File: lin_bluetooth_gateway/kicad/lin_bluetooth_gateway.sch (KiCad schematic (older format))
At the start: 9 parts, among them P1 MOLEX-0431603103, P2 MOLEX-0431603103, P4 CONN_01X03, U1 MCP2050, U2 BL652

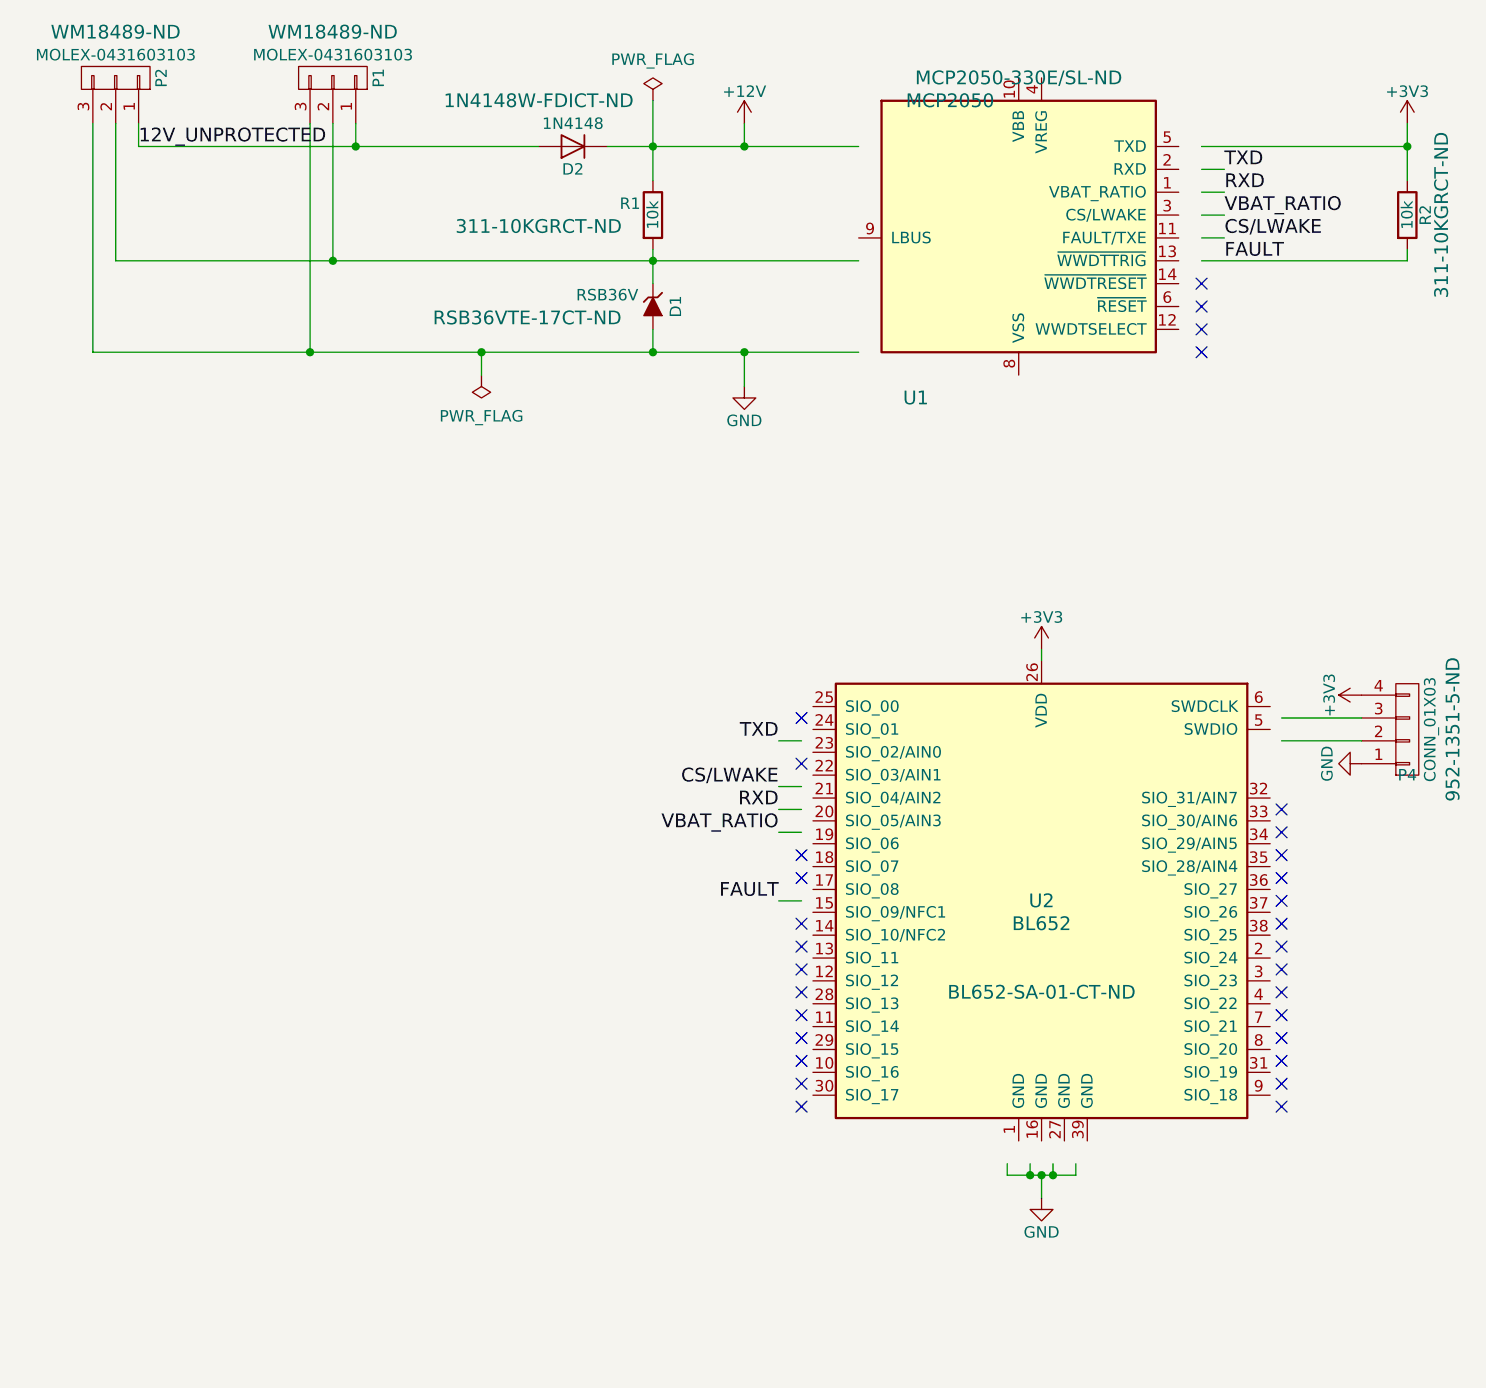
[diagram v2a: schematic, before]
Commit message: Moving MCP2050 symbol to "microchip" library
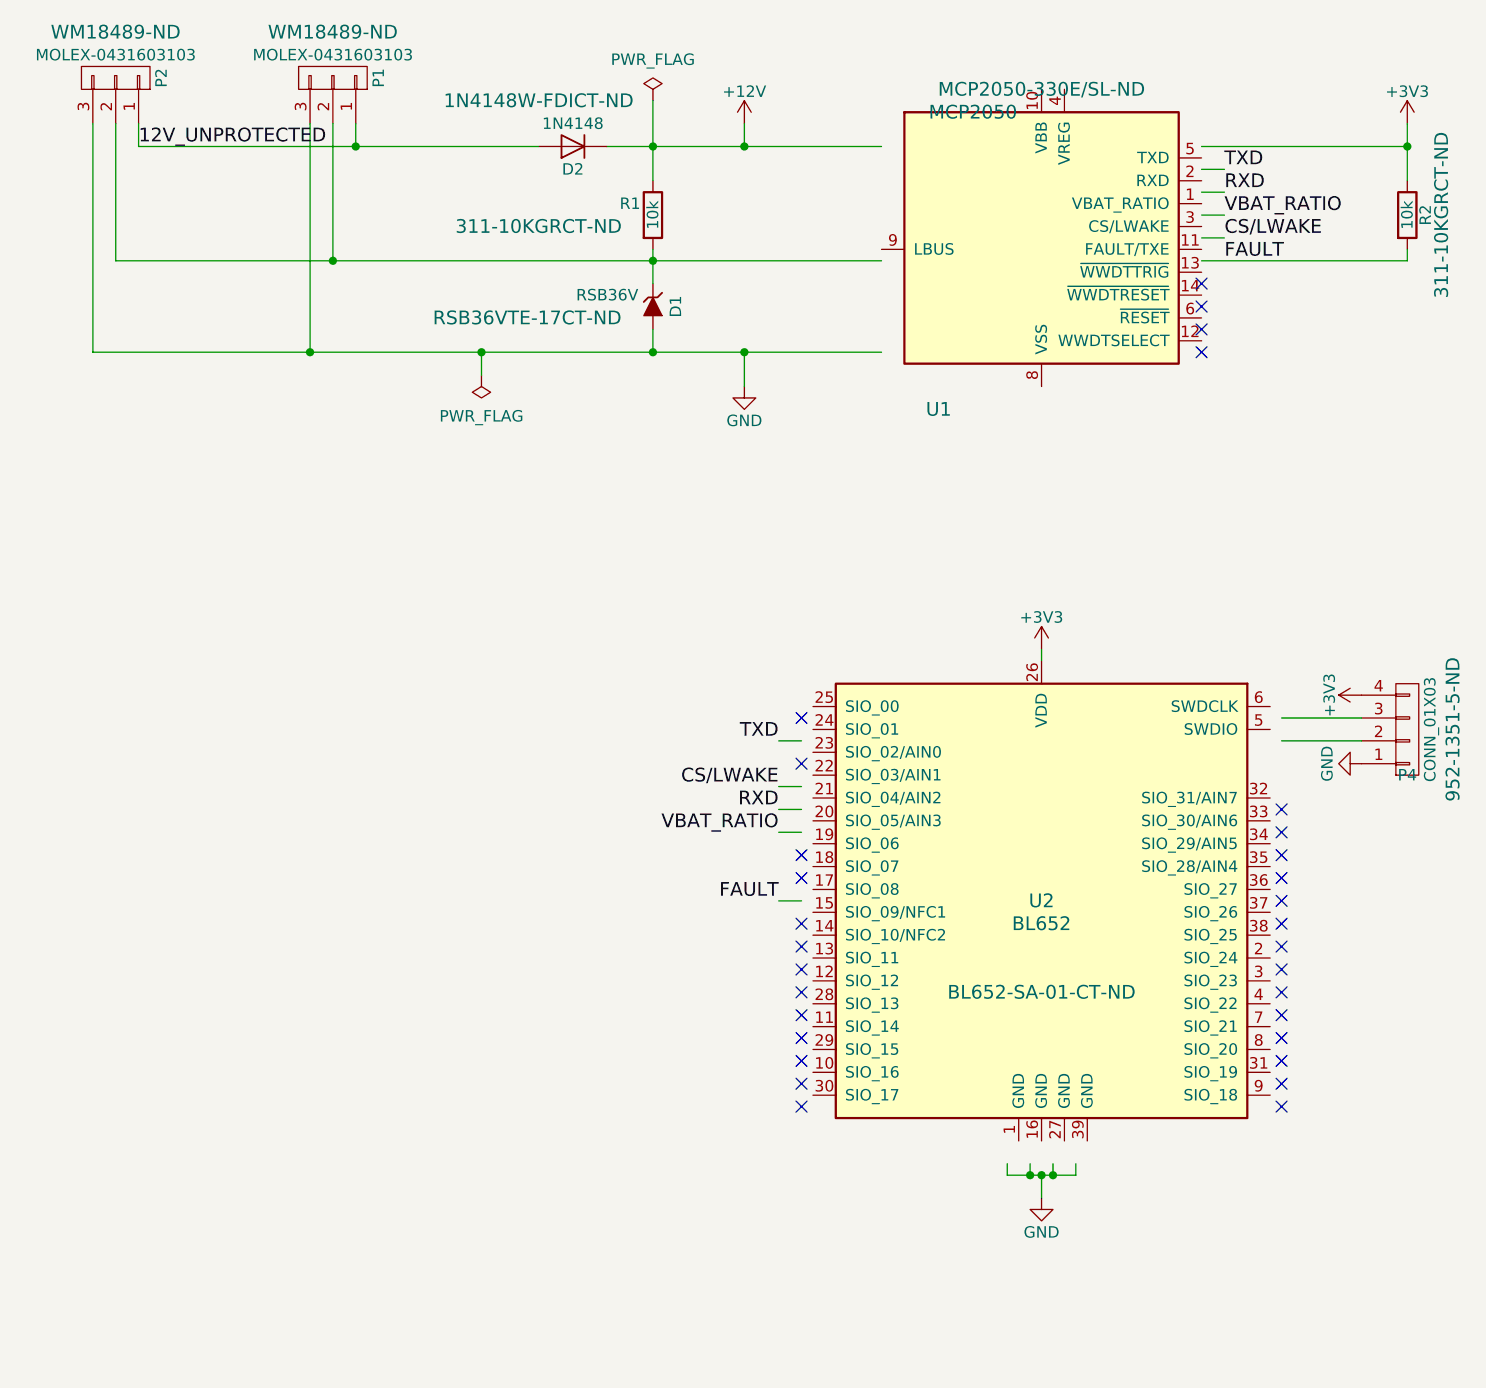
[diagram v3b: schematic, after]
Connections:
- wire segments 38 -> 53
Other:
- moved on the sheet: U1
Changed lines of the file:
@@
 LIBS:valves
 LIBS:laird
-LIBS:mcp2050
 LIBS:lin_bluetooth_gateway-cache
 EELAYER 25 0
@@
 L MCP2050 U1
 U 1 1 5807224D
-P 5350 1850
-F 0 "U1" H 4900 1150 60  0000 C CNN
-F 1 "MCP2050" H 5050 2450 60  0000 C CNN
-F 2 "Housings_SOIC:SOIC-14_3.9x8.7mm_Pitch1.27mm" H 4900 1900 60  0001 C CNN
-F 3 "http://ww1.microchip.com/downloads/en/DeviceDoc/22299B.pdf" H 4900 1900 60  0001 C CNN
-F 4 "MCP2050-330E/SL-ND" H 5350 2550 60  0000 C CNN "DIGIKEY"
-	1    5350 1850
-	1    0    0    -1
-$EndComp
-Wire Wire Line
-	1300 2350 4650 2350
+P 5450 1900
+F 0 "U1" H 5000 1200 60  0000 C CNN
+F 1 "MCP2050" H 5150 2500 60  0000 C CNN
+F 2 "Housings_SOIC:SOIC-14_3.9x8.7mm_Pitch1.27mm" H 5000 1950 60  0001 C CNN
+F 3 "http://ww1.microchip.com/downloads/en/DeviceDoc/22299B.pdf" H 5000 1950 60  0001 C CNN
+F 4 "MCP2050-330E/SL-ND" H 5450 2600 60  0000 C CNN "DIGIKEY"
+	1    5450 1900
+	1    0    0    -1
+$EndComp
+Wire Wire Line
+	1300 2350 2250 2350
+Wire Wire Line
+	2250 2350 3000 2350
+Wire Wire Line
+	3000 2350 3750 2350
+Wire Wire Line
+	3750 2350 4150 2350
+Wire Wire Line
+	4150 2350 4750 2350
 Wire Wire Line
 	4150 2350 4150 2500
@@
 	6250 1750 6150 1750
 Wire Wire Line
-	3550 1450 4650 1450
-Wire Wire Line
-	1400 1950 4650 1950
+	3550 1450 3750 1450
+Wire Wire Line
+	3750 1450 4150 1450
+Wire Wire Line
+	4150 1450 4750 1450
+Wire Wire Line
+	1400 1950 2350 1950
+Wire Wire Line
+	2350 1950 3750 1950
+Wire Wire Line
+	3750 1950 4750 1950
 Connection ~ 4150 2350
 $Comp
@@
 	7050 1900 7050 1950
 Wire Wire Line
-	7050 1350 7050 1600
+	7050 1350 7050 1450
+Wire Wire Line
+	7050 1450 7050 1600
 Connection ~ 7050 1450
 $Comp
@@
 $EndComp
 Wire Wire Line
-	3750 1900 3750 2050
+	3750 1900 3750 1950
+Wire Wire Line
+	3750 1950 3750 2050
 Connection ~ 3750 1950
 $Comp
@@
 $EndComp
 Wire Wire Line
-	3750 1250 3750 1600
+	3750 1250 3750 1450
+Wire Wire Line
+	3750 1450 3750 1600
 $Comp
 L CONN_01X03 P1
@@
 $EndComp
 Wire Wire Line
-	1500 1450 3250 1450
+	1500 1450 2450 1450
+Wire Wire Line
+	2450 1450 3250 1450
 Connection ~ 3750 1450
 Wire Wire Line
@@
 	5300 5900 5300 5950
 Wire Wire Line
-	5300 5950 5600 5950
+	5300 5950 5400 5950
+Wire Wire Line
+	5400 5950 5450 5950
+Wire Wire Line
+	5450 5950 5500 5950
+Wire Wire Line
+	5500 5950 5600 5950
 Wire Wire Line
 	5600 5950 5600 5900

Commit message: Using BL652 from rfcomm library
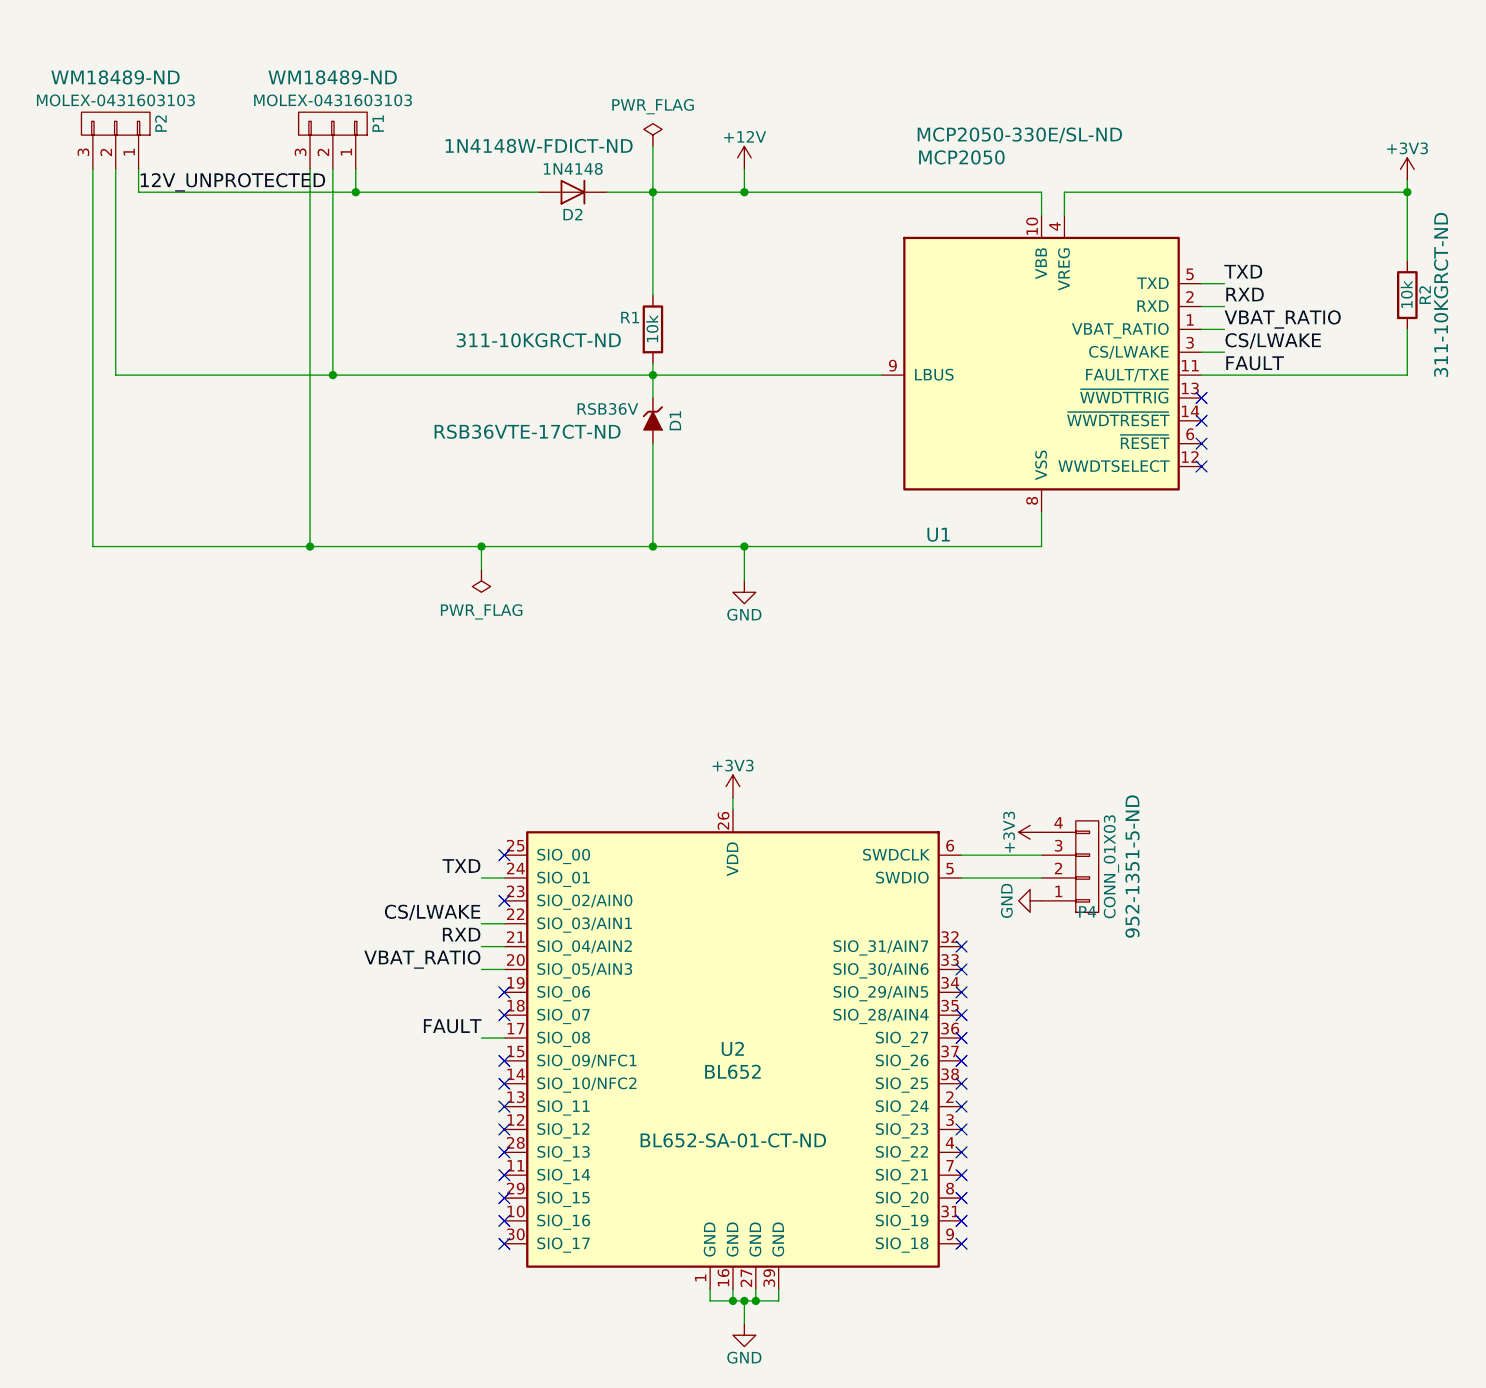
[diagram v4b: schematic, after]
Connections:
- wire segments 53 -> 41
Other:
- moved on the sheet: D1, D2, P1, P2, P4, R1, R2, U1, U2

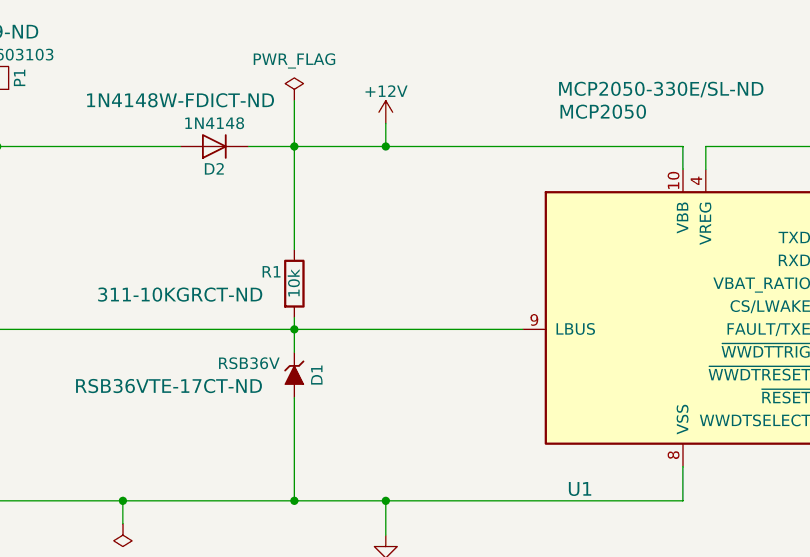
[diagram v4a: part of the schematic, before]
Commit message: First working NRF52 master with two slave PIC nodes
# Software

* Using LIN 2.x checksum instead of LIN 1.x
* Using 19200 baudrate instead of 20000 for compatibility with NRF52
* Setting only the NRF52 as master
* Deactivating sleep mode for PIC as it was broken
* Ignoring break signal (not generated by NRF52 yet)
* Code cleaning: removing unused functions

# Boards

* Updating Git submodules
* Moving text references for the 8x input board
* Adding a TODO note for replacing the LIN pull-up resistor
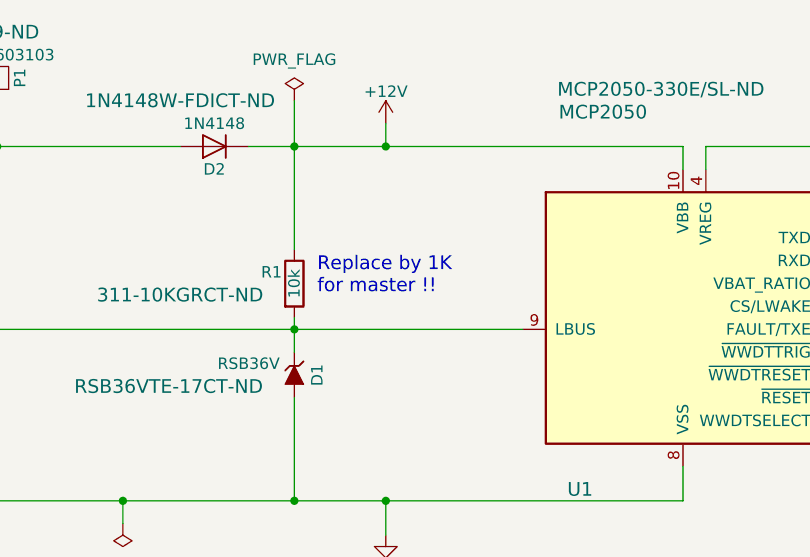
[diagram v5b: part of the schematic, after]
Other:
- note added: "Replace by 1K\nfor master !!"
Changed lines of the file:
@@
 Wire Wire Line
 	5450 3200 5450 3050
+Text Notes 3850 2300 0    60   ~ 0
+Replace by 1K\nfor master !!
 $EndSCHEMATC
